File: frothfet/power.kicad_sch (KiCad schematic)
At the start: 43 parts, among them J10 Screw_Terminal_01x08, J11 Screw_Terminal_01x08, U26 TPS7A2033PDBVR, U27 XL1509-5.0, U28 MCP3425A0T-ECH, U29 MAX40200AUK

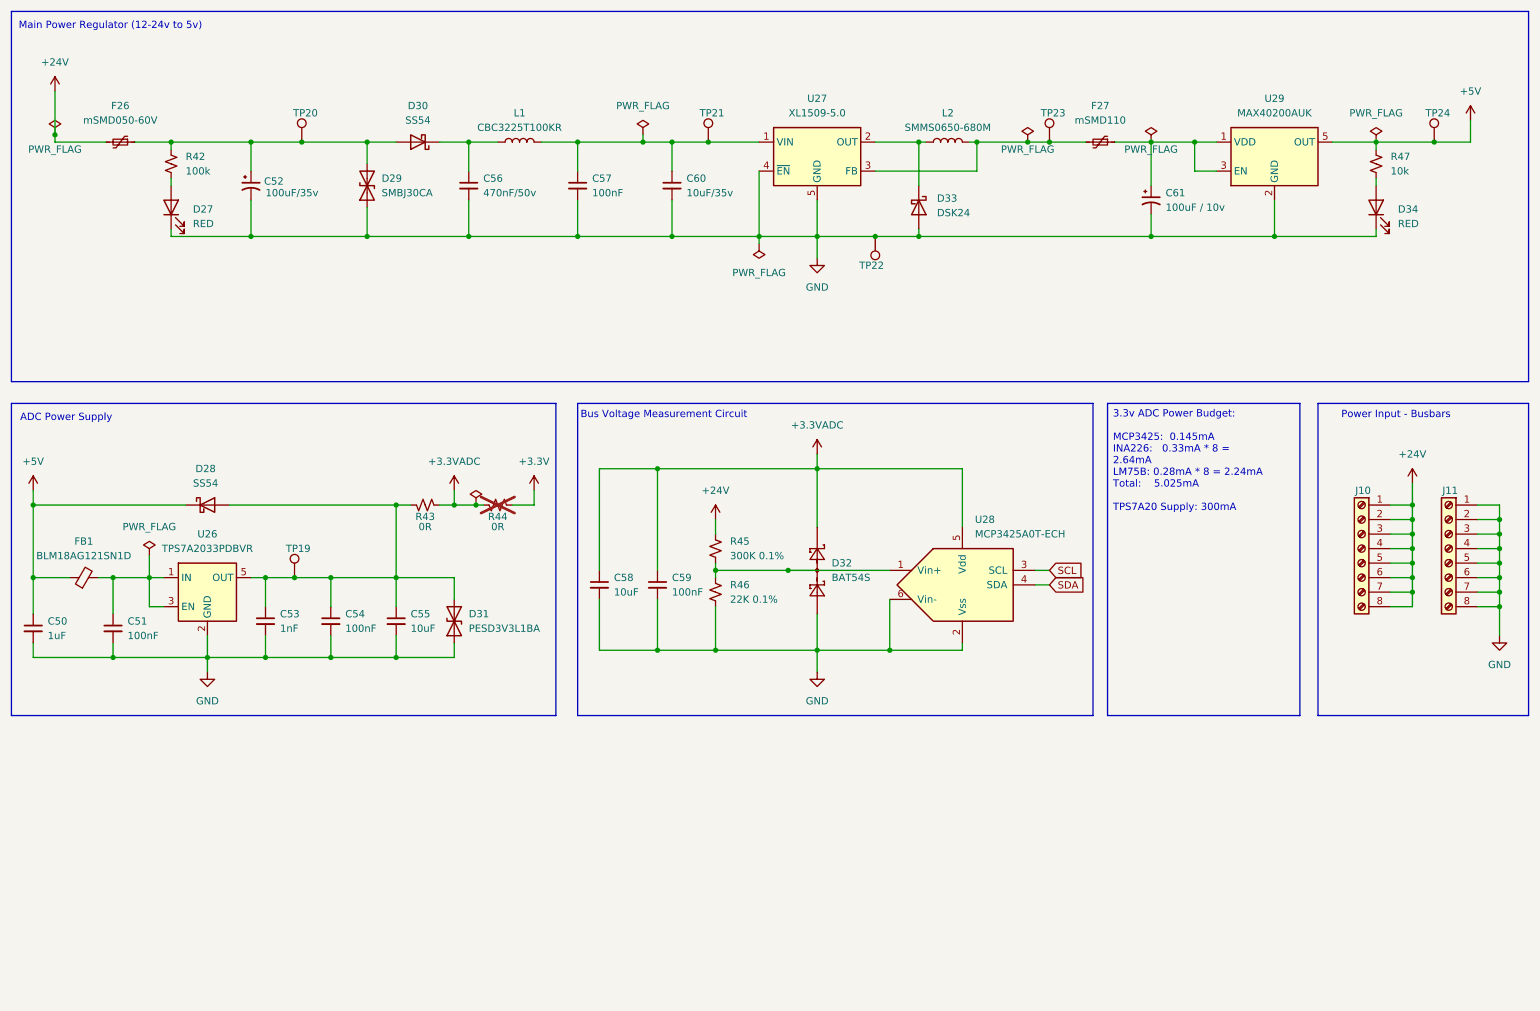
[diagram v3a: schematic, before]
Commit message: channel routing is basically done
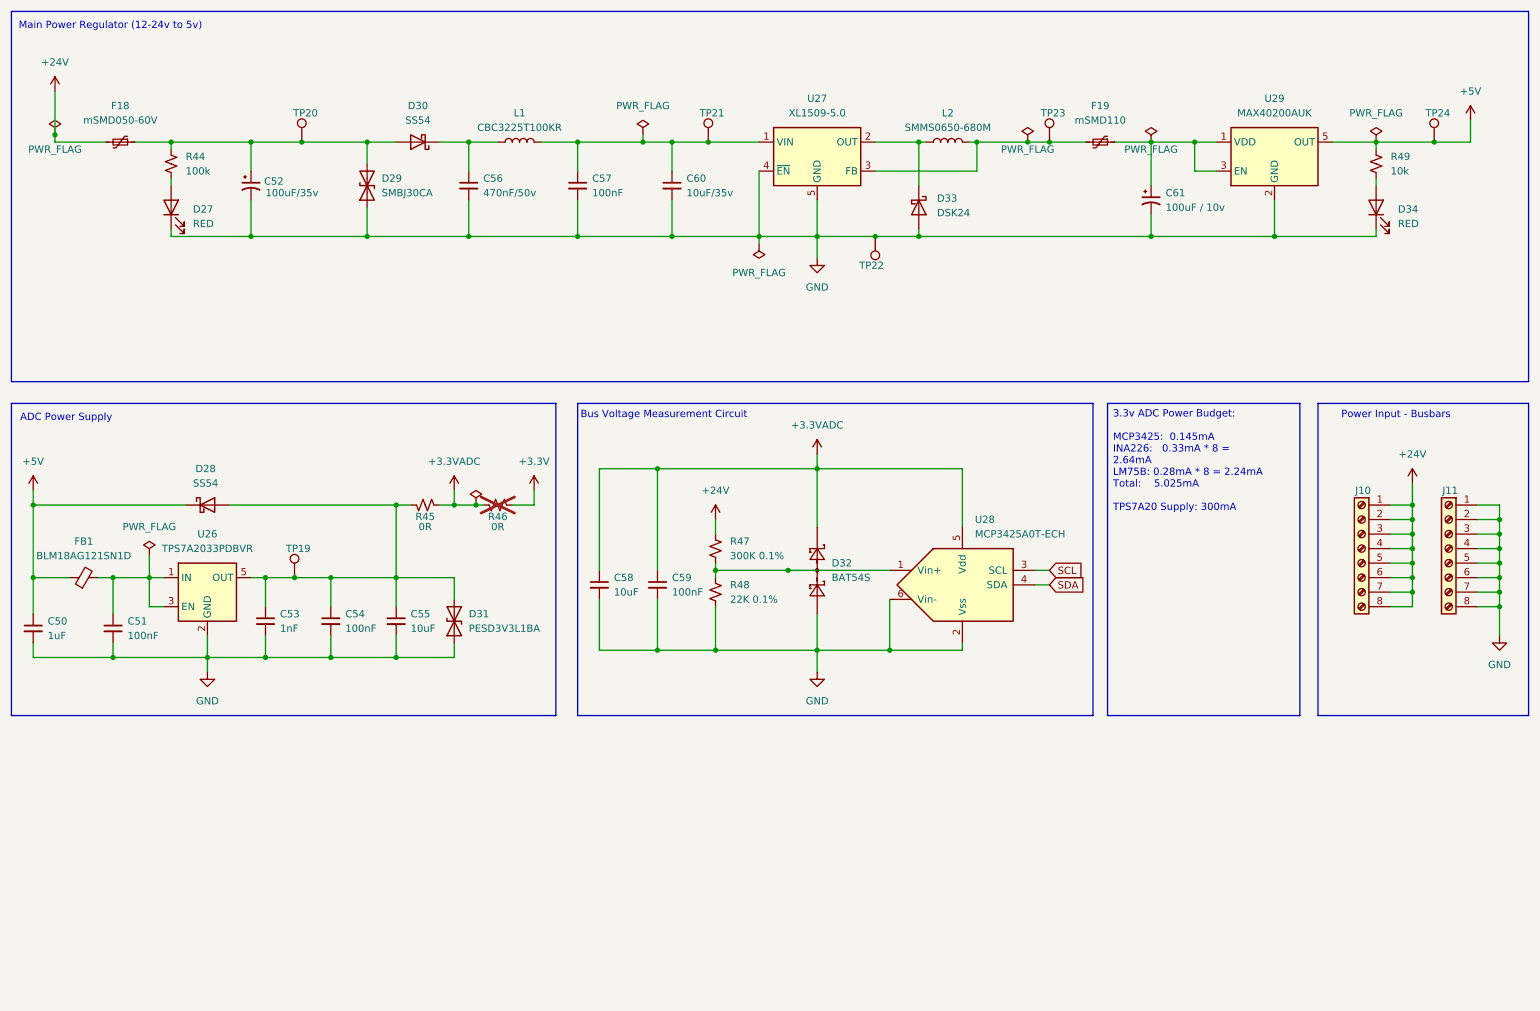
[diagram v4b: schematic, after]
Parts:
- renumbered F26 to F18, F27 to F19, R42 to R44, R43 to R45, R44 to R46, R45 to R47, R46 to R48, R47 to R49
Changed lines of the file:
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@@
 		(dnp no)
 		(fields_autoplaced yes)
-		(property "Reference" "R42"
+		(property "Reference" "R44"
 			(at 45.72 40.6399 0)
 			(effects
@@
 			(project "frothfet"
 				(path "/c83c6236-96e9-46ad-9d7a-9e2efa4a7966/e112a34f-fd2f-43cb-bf5d-a7f5e57b6bef"
-					(reference "R42")
+					(reference "R44")
 					(unit 1)
 				)
@@
 		(dnp no)
 		(fields_autoplaced yes)
-		(property "Reference" "R47"
+		(property "Reference" "R49"
 			(at 256.54 40.6399 0)
 			(effects
@@
 			(project "frothfet"
 				(path "/c83c6236-96e9-46ad-9d7a-9e2efa4a7966/e112a34f-fd2f-43cb-bf5d-a7f5e57b6bef"
-					(reference "R47")
+					(reference "R49")
 					(unit 1)
 				)
@@
 		(dnp no)
 		(fields_autoplaced yes)
-		(property "Reference" "R45"
+		(property "Reference" "R47"
 			(at 140.97 107.95 0)
 			(effects
@@
 			(project "8ch-mosfet"
 				(path "/c83c6236-96e9-46ad-9d7a-9e2efa4a7966/e112a34f-fd2f-43cb-bf5d-a7f5e57b6bef"
-					(reference "R45")
+					(reference "R47")
 					(unit 1)
 				)
@@
 		(dnp no)
 		(fields_autoplaced yes)
-		(property "Reference" "F27"
+		(property "Reference" "F19"
 			(at 205.74 31.75 90)
 			(effects
@@
 			(project "8ch-mosfet"
 				(path "/c83c6236-96e9-46ad-9d7a-9e2efa4a7966/e112a34f-fd2f-43cb-bf5d-a7f5e57b6bef"
-					(reference "F27")
+					(reference "F19")
 					(unit 1)
 				)
@@
 		(dnp no)
 		(fields_autoplaced yes)
-		(property "Reference" "F26"
+		(property "Reference" "F18"
 			(at 34.29 31.75 90)
 			(effects
@@
 			(project "8ch-mosfet"
 				(path "/c83c6236-96e9-46ad-9d7a-9e2efa4a7966/e112a34f-fd2f-43cb-bf5d-a7f5e57b6bef"
-					(reference "F26")
+					(reference "F18")
 					(unit 1)
 				)
@@
 		(on_board yes)
 		(dnp no)
-		(property "Reference" "R43"
+		(property "Reference" "R45"
 			(at 87.63 103.632 90)
 			(effects
@@
 			(project "frothfet"
 				(path "/c83c6236-96e9-46ad-9d7a-9e2efa4a7966/e112a34f-fd2f-43cb-bf5d-a7f5e57b6bef"
-					(reference "R43")
+					(reference "R45")
 					(unit 1)
 				)
@@
 		(on_board yes)
 		(dnp yes)
-		(property "Reference" "R44"
+		(property "Reference" "R46"
 			(at 100.33 103.632 90)
 			(effects
@@
 			(project "frothfet"
 				(path "/c83c6236-96e9-46ad-9d7a-9e2efa4a7966/e112a34f-fd2f-43cb-bf5d-a7f5e57b6bef"
-					(reference "R44")
+					(reference "R46")
 					(unit 1)
 				)
@@
 		(dnp no)
 		(fields_autoplaced yes)
-		(property "Reference" "R46"
+		(property "Reference" "R48"
 			(at 140.97 115.57 0)
 			(effects
@@
 			(project "8ch-mosfet"
 				(path "/c83c6236-96e9-46ad-9d7a-9e2efa4a7966/e112a34f-fd2f-43cb-bf5d-a7f5e57b6bef"
-					(reference "R46")
+					(reference "R48")
 					(unit 1)
 				)

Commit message: starting to layout the rest of the components.
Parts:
- renumbered J10 to J11, J11 to J12
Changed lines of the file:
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@@
 		(on_board yes)
 		(dnp no)
-		(property "Reference" "J10"
+		(property "Reference" "J11"
 			(at 251.714 99.06 0)
 			(effects
@@
 			(project ""
 				(path "/c83c6236-96e9-46ad-9d7a-9e2efa4a7966/e112a34f-fd2f-43cb-bf5d-a7f5e57b6bef"
-					(reference "J10")
+					(reference "J11")
 					(unit 1)
 				)
@@
 		(dnp no)
 		(fields_autoplaced yes)
-		(property "Reference" "#PWR0125"
+		(property "Reference" "#PWR0127"
 			(at 19.05 102.87 0)
 			(effects
@@
 			(project "frothfet"
 				(path "/c83c6236-96e9-46ad-9d7a-9e2efa4a7966/e112a34f-fd2f-43cb-bf5d-a7f5e57b6bef"
-					(reference "#PWR0125")
+					(reference "#PWR0127")
 					(unit 1)
 				)
@@
 		(dnp no)
 		(fields_autoplaced yes)
-		(property "Reference" "#PWR0129"
+		(property "Reference" "#PWR0131"
 			(at 106.68 102.87 0)
 			(effects
@@
 			(project "frothfet"
 				(path "/c83c6236-96e9-46ad-9d7a-9e2efa4a7966/e112a34f-fd2f-43cb-bf5d-a7f5e57b6bef"
-					(reference "#PWR0129")
+					(reference "#PWR0131")
 					(unit 1)
 				)
@@
 		(dnp no)
 		(fields_autoplaced yes)
-		(property "Reference" "#PWR0133"
+		(property "Reference" "#PWR0135"
 			(at 156.21 137.16 0)
 			(effects
@@
 			(project "frothfet"
 				(path "/c83c6236-96e9-46ad-9d7a-9e2efa4a7966/e112a34f-fd2f-43cb-bf5d-a7f5e57b6bef"
-					(reference "#PWR0133")
+					(reference "#PWR0135")
 					(unit 1)
 				)
@@
 		(dnp no)
 		(fields_autoplaced yes)
-		(property "Reference" "#PWR0128"
+		(property "Reference" "#PWR0130"
 			(at 88.9 100.33 0)
 			(effects
@@
 			(project ""
 				(path "/c83c6236-96e9-46ad-9d7a-9e2efa4a7966/e112a34f-fd2f-43cb-bf5d-a7f5e57b6bef"
-					(reference "#PWR0128")
+					(reference "#PWR0130")
 					(unit 1)
 				)
@@
 		(on_board yes)
 		(dnp no)
-		(property "Reference" "J11"
+		(property "Reference" "J12"
 			(at 266.954 99.06 0)
 			(effects
@@
 			(project ""
 				(path "/c83c6236-96e9-46ad-9d7a-9e2efa4a7966/e112a34f-fd2f-43cb-bf5d-a7f5e57b6bef"
-					(reference "J11")
+					(reference "J12")
 					(unit 1)
 				)
@@
 		(dnp no)
 		(fields_autoplaced yes)
-		(property "Reference" "#PWR0130"
+		(property "Reference" "#PWR0132"
 			(at 138.43 107.95 0)
 			(effects
@@
 			(project "8ch-mosfet"
 				(path "/c83c6236-96e9-46ad-9d7a-9e2efa4a7966/e112a34f-fd2f-43cb-bf5d-a7f5e57b6bef"
-					(reference "#PWR0130")
+					(reference "#PWR0132")
 					(unit 1)
 				)
@@
 		(dnp no)
 		(fields_autoplaced yes)
-		(property "Reference" "#PWR0136"
+		(property "Reference" "#PWR0138"
 			(at 275.59 130.81 0)
 			(effects
@@
 			(project "8ch-mosfet"
 				(path "/c83c6236-96e9-46ad-9d7a-9e2efa4a7966/e112a34f-fd2f-43cb-bf5d-a7f5e57b6bef"
-					(reference "#PWR0136")
+					(reference "#PWR0138")
 					(unit 1)
 				)
@@
 		(dnp no)
 		(fields_autoplaced yes)
-		(property "Reference" "#PWR0134"
+		(property "Reference" "#PWR0136"
 			(at 260.35 101.6 0)
 			(effects
@@
 			(project "8ch-mosfet"
 				(path "/c83c6236-96e9-46ad-9d7a-9e2efa4a7966/e112a34f-fd2f-43cb-bf5d-a7f5e57b6bef"
-					(reference "#PWR0134")
+					(reference "#PWR0136")
 					(unit 1)
 				)
@@
 		(dnp no)
 		(fields_autoplaced yes)
-		(property "Reference" "#PWR0131"
+		(property "Reference" "#PWR0133"
 			(at 156.21 64.77 0)
 			(effects
@@
 			(project "8ch-mosfet"
 				(path "/c83c6236-96e9-46ad-9d7a-9e2efa4a7966/e112a34f-fd2f-43cb-bf5d-a7f5e57b6bef"
-					(reference "#PWR0131")
+					(reference "#PWR0133")
 					(unit 1)
 				)
@@
 		(dnp no)
 		(fields_autoplaced yes)
-		(property "Reference" "#PWR0135"
+		(property "Reference" "#PWR0137"
 			(at 270.51 38.1 0)
 			(effects
@@
 			(project "8ch-mosfet"
 				(path "/c83c6236-96e9-46ad-9d7a-9e2efa4a7966/e112a34f-fd2f-43cb-bf5d-a7f5e57b6bef"
-					(reference "#PWR0135")
+					(reference "#PWR0137")
 					(unit 1)
 				)
@@
 		(dnp no)
 		(fields_autoplaced yes)
-		(property "Reference" "#PWR0127"
+		(property "Reference" "#PWR0129"
 			(at 49.53 137.16 0)
 			(effects
@@
 			(project ""
 				(path "/c83c6236-96e9-46ad-9d7a-9e2efa4a7966/e112a34f-fd2f-43cb-bf5d-a7f5e57b6bef"
-					(reference "#PWR0127")
+					(reference "#PWR0129")
 					(unit 1)
 				)
@@
 		(dnp no)
 		(fields_autoplaced yes)
-		(property "Reference" "#PWR0126"
+		(property "Reference" "#PWR0128"
 			(at 22.86 33.02 0)
 			(effects
@@
 			(project "8ch-mosfet"
 				(path "/c83c6236-96e9-46ad-9d7a-9e2efa4a7966/e112a34f-fd2f-43cb-bf5d-a7f5e57b6bef"
-					(reference "#PWR0126")
+					(reference "#PWR0128")
 					(unit 1)
 				)
@@
 		(dnp no)
 		(fields_autoplaced yes)
-		(property "Reference" "#PWR0132"
+		(property "Reference" "#PWR0134"
 			(at 160.02 93.98 0)
 			(effects
@@
 			(project "frothfet"
 				(path "/c83c6236-96e9-46ad-9d7a-9e2efa4a7966/e112a34f-fd2f-43cb-bf5d-a7f5e57b6bef"
-					(reference "#PWR0132")
+					(reference "#PWR0134")
 					(unit 1)
 				)

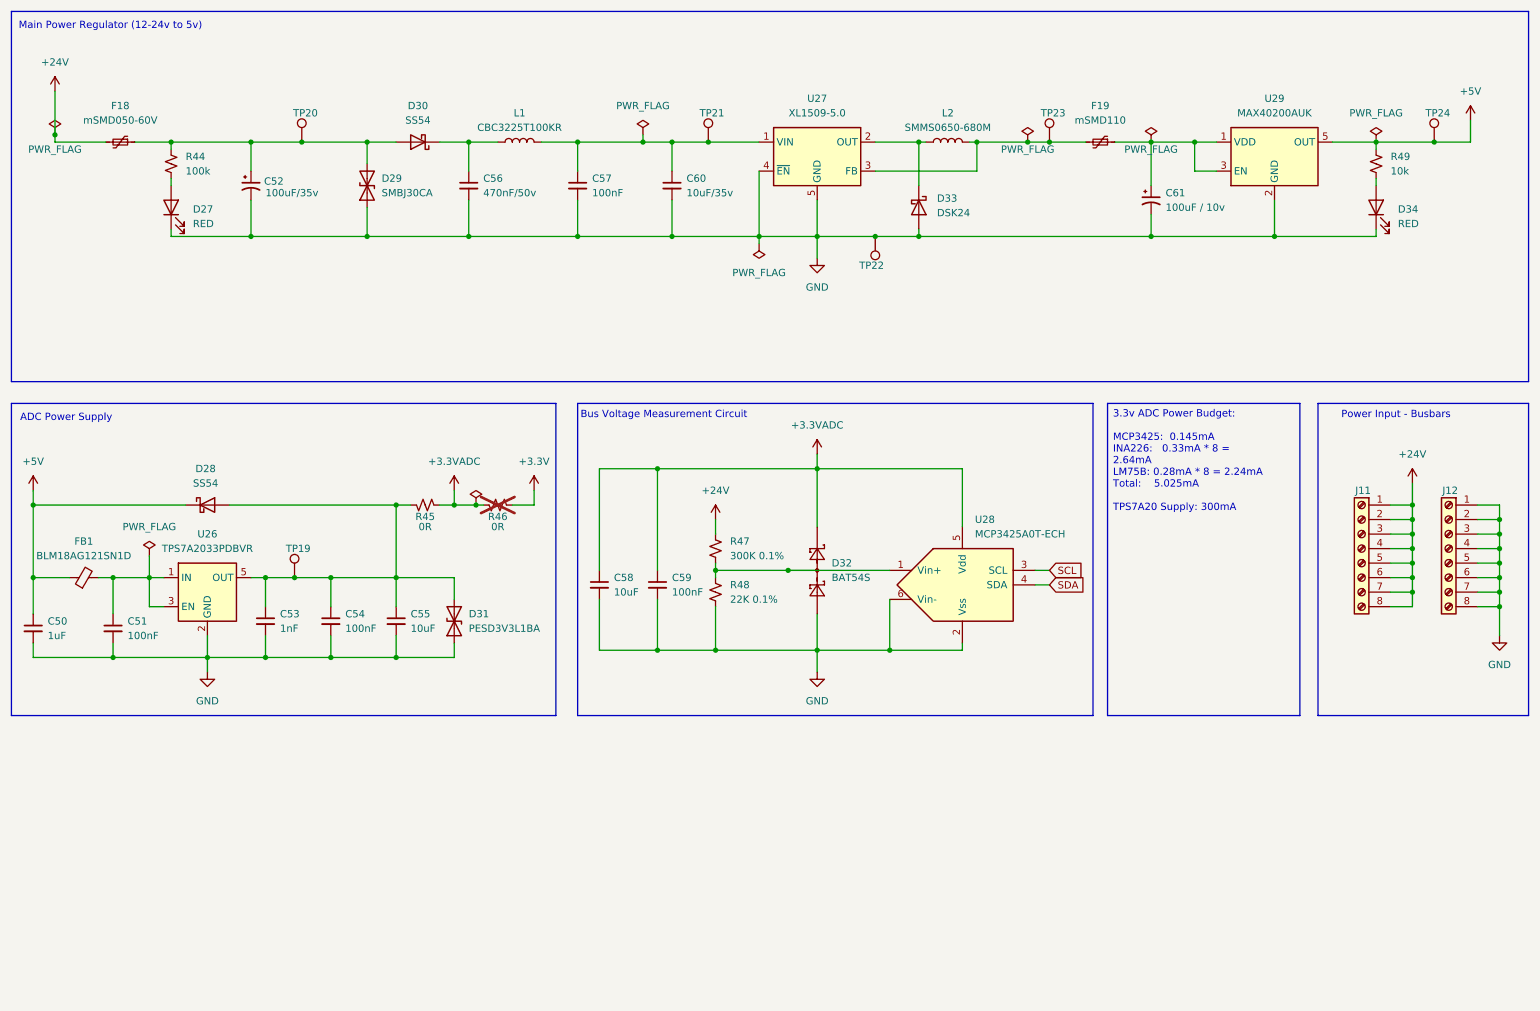
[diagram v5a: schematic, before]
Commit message: mostly routed
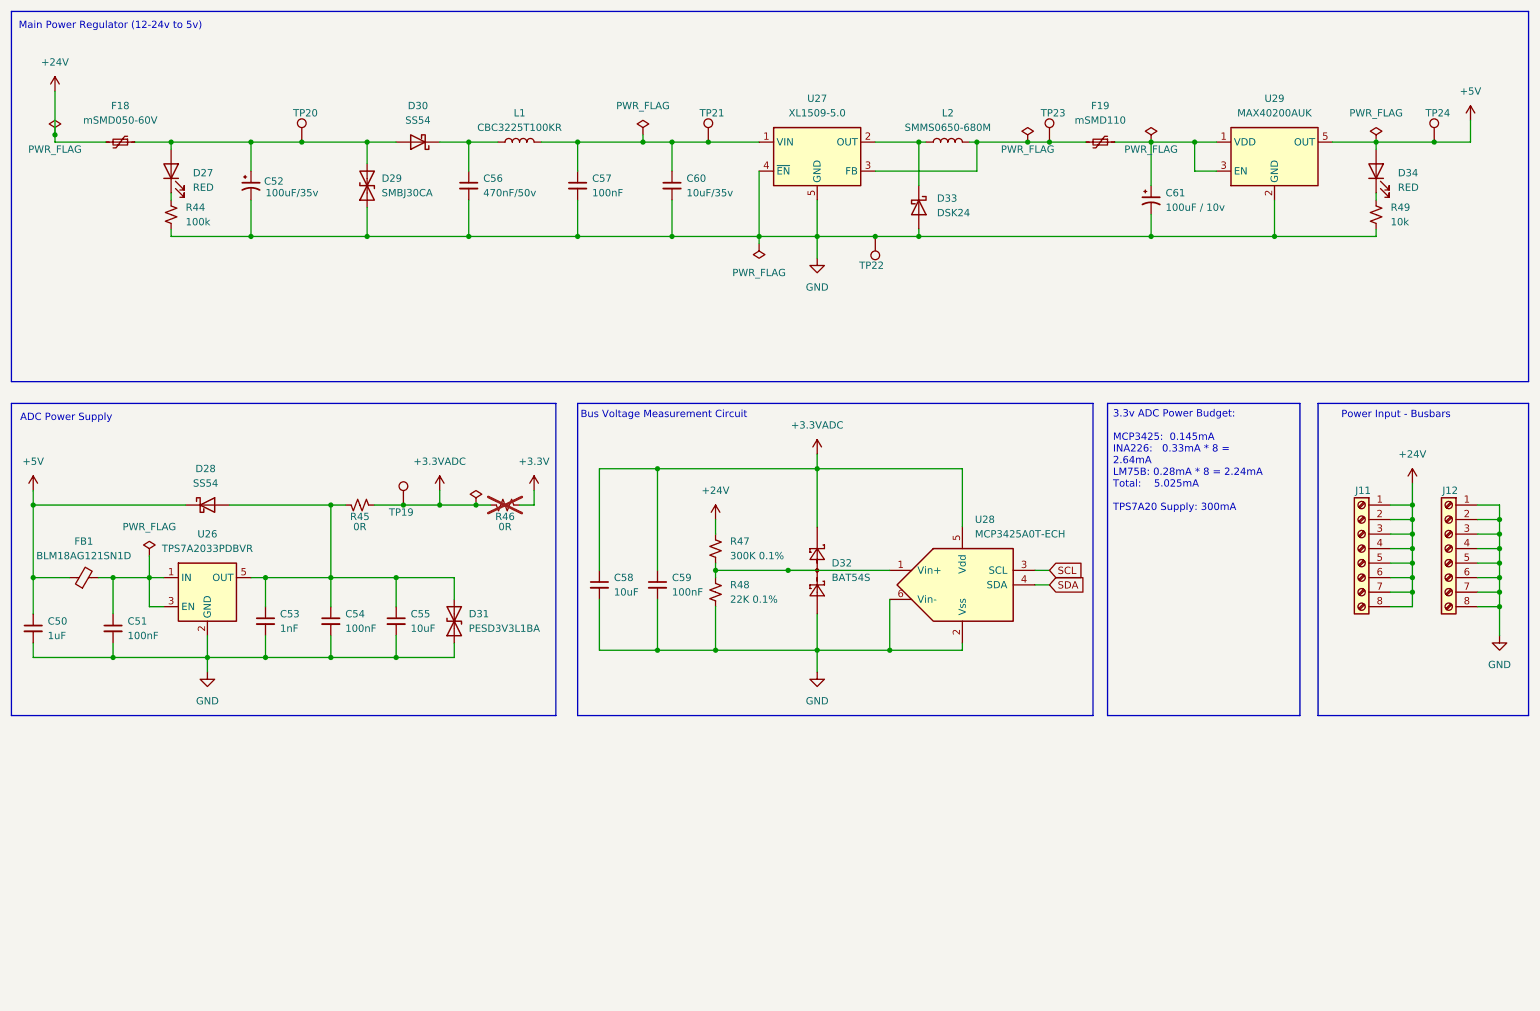
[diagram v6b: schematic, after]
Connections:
- net +3.3VADC: now also TP19.1
- net +5V: now also D34.2 (A); no longer R49.1
- net GND: now also R44.2, R49.2; no longer D27.1 (K), D34.1 (K)
- net at C53.1, C54.1, C55.1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: no longer TP19.1
- net at C52.1, D29.2 (A2), D30.2 (A)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: now also D27.2 (A); no longer R44.1
- new net: D27.1 (K), R44.1
- new net: D34.1 (K), R49.1
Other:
- moved on the sheet: D27, D34, R44, R45, R46, R49, TP19
